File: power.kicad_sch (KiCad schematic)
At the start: 55 parts, among them T1 net-tie, U1 LMR54410, U11 RT9080-33GJ5, U3 TPS546D24ARVFR, U5 MIC5504

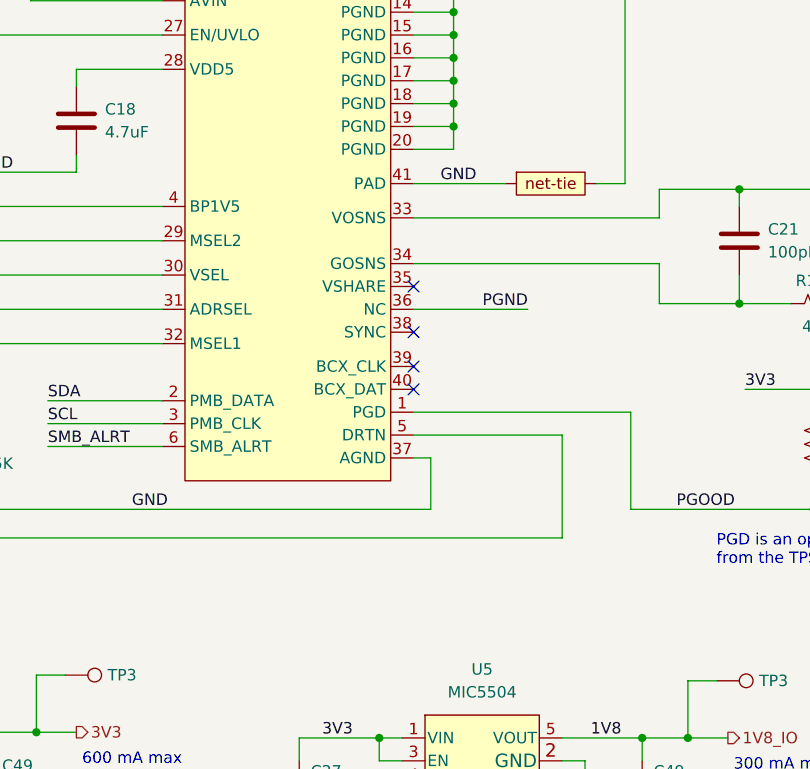
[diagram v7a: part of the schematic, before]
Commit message: lots of power supply routing
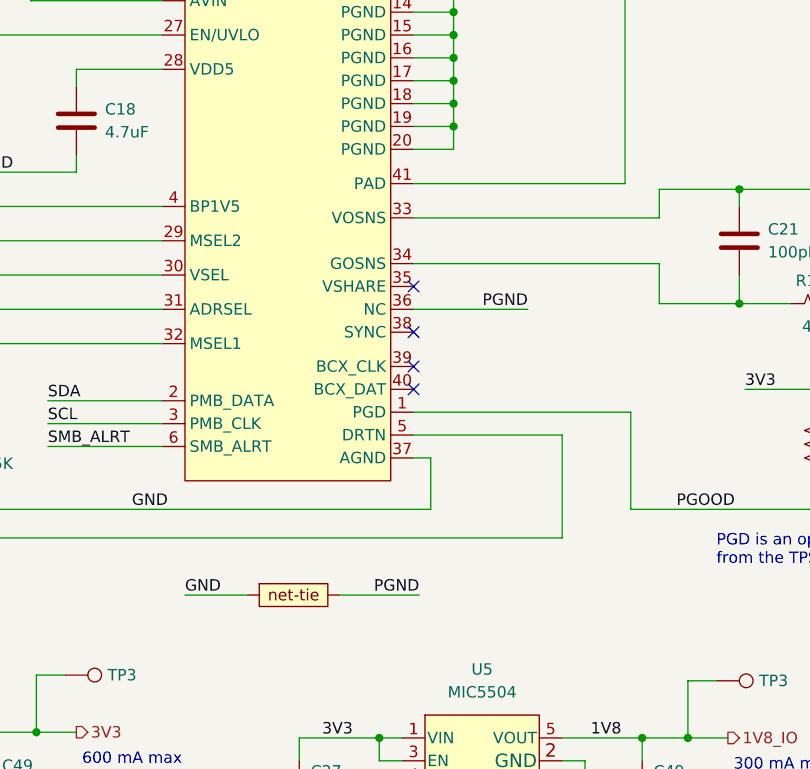
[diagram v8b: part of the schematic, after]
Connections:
- net GND: no longer U3.41 (PAD)
- net PGND: now also U3.41 (PAD)
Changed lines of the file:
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@@
-    (stroke (width 0) (type default))
-  )
-  (wire (pts (xy 178.435 80.01) (xy 181.61 80.01))
     (stroke (width 0) (type default))
   )
@@
     (stroke (width 0) (type default))
   )
+  (wire (pts (xy 158.115 80.01) (xy 181.61 80.01))
+    (stroke (width 0) (type default))
+  )
   (wire (pts (xy 97.155 113.665) (xy 97.155 116.205))
     (stroke (width 0) (type default))
@@
     (stroke (width 0) (type default))
   )
+  (wire (pts (xy 132.715 125.73) (xy 139.7 125.73))
+    (stroke (width 0) (type default))
+  )
   (wire (pts (xy 235.585 93.345) (xy 247.65 93.345))
     (stroke (width 0) (type default))
@@
     (stroke (width 0) (type default))
   )
-  (wire (pts (xy 158.115 80.01) (xy 168.275 80.01))
-    (stroke (width 0) (type default))
-  )
   (wire (pts (xy 89.535 20.32) (xy 78.74 20.32))
     (stroke (width 0) (type default))
@@
   )
   (wire (pts (xy 67.945 20.32) (xy 57.15 20.32))
+    (stroke (width 0) (type default))
+  )
+  (wire (pts (xy 149.86 125.73) (xy 158.75 125.73))
     (stroke (width 0) (type default))
   )
@@
     (effects (font (size 1.27 1.27)) (justify left bottom))
   )
-  (label "GND" (at 165.1 80.01 180) (fields_autoplaced)
-    (effects (font (size 1.27 1.27)) (justify right bottom))
+  (label "GND" (at 132.715 125.73 0) (fields_autoplaced)
+    (effects (font (size 1.27 1.27)) (justify left bottom))
   )
   (label "GND" (at 163.195 154.94 0) (fields_autoplaced)
@@
   )
   (label "PGND" (at 174.625 58.42 180) (fields_autoplaced)
+    (effects (font (size 1.27 1.27)) (justify right bottom))
+  )
+  (label "PGND" (at 158.75 125.73 180) (fields_autoplaced)
     (effects (font (size 1.27 1.27)) (justify right bottom))
   )
@@
     )
   )
-  (symbol (lib_id "bitaxe:net-tie") (at 173.355 80.01 0) (unit 1)
+  (symbol (lib_id "bitaxe:net-tie") (at 144.78 125.73 0) (unit 1)
     (in_bom yes) (on_board yes) (dnp no)
-    (property "Reference" "T1" (at 169.545 74.93 0)
-      (effects (font (size 1.27 1.27)) hide)
-    )
-    (property "Value" "net-tie" (at 173.355 77.47 0)
-      (effects (font (size 1.27 1.27)) hide)
-    )
-    (property "Footprint" "" (at 172.085 81.28 0)
-      (effects (font (size 1.27 1.27)) hide)
-    )
-    (property "Datasheet" "" (at 172.085 81.28 0)
-      (effects (font (size 1.27 1.27)) hide)
-    )
+    (property "Reference" "T1" (at 140.97 120.65 0)
+      (effects (font (size 1.27 1.27)) hide)
+    )
+    (property "Value" "net-tie" (at 144.78 123.19 0)
+      (effects (font (size 1.27 1.27)) hide)
+    )
+    (property "Footprint" "" (at 143.51 127 0)
+      (effects (font (size 1.27 1.27)) hide)
+    )
+    (property "Datasheet" "" (at 143.51 127 0)
+      (effects (font (size 1.27 1.27)) hide)
+    )
